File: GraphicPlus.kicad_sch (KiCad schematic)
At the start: 23 parts, among them J1 Apple II Expansion Bus, J2 Printer Connector, Q1 Q_NPN_EBC, SW1 SW_DIP_x04, U1 74LS00, U10 74LS373, U11 74LS373, U2 74LS279, U3 74LS02, U4 74LS00, U5 74LS74, U6 74LS00, U7 74LS08, U8 74LS30, U9 2732

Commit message: native 374 version
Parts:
- removed Q1: Q_NPN_EBC, Package_TO_SOT_THT:TO-92, symbol Device:Q_NPN_EBC
- removed R2: 4.7K, Resistor_THT:R_Axial_DIN0207_L6.3mm_D2.5mm_P10.16mm_Horizontal, symbol Device:R
- removed U4: 74LS00, Package_DIP:DIP-14_W7.62mm, symbol 74xx:74LS00
- added C7, C8: C, Capacitor_THT:C_Rect_L7.0mm_W2.0mm_P5.00mm, symbol Device:C
- C1: value C -> 100p
- C3: value C -> 470p
- D1: footprint Diode_THT:D_A-405_P10.16mm_Horizontal -> Diode_THT:D_A-405_P7.62mm_Horizontal
- U9: value 2732 -> 2764; footprint Package_DIP:DIP-24_W15.24mm -> Package_DIP:DIP-28_W15.24mm; symbol MyEprom:2732 -> Memory_EPROM:2764
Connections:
- net +5V: now also U11.18 (D7), U2.1 (~{R}), U2.2 (~{S1}), U2.3 (~{S2}), U9.1 (VPP), U9.27 (~{PGM}), U9.28 (VCC), C8.1; no longer U9.24 (VCC)
- net A0: now also U9.10 (A0); no longer U9.8 (A0)
- net A1: now also U9.9 (A1); no longer U1.5, U9.7 (A1)
- net A2: now also U9.8 (A2); no longer U1.1, U9.6 (A2)
- net A3: now also U9.7 (A3); no longer U9.5 (A3)
- net A4: now also U9.6 (A4); no longer U9.4 (A4)
- net A5: now also U9.5 (A5); no longer U9.3 (A5)
- net A7: now also U9.3 (A7); no longer U9.1 (A7)
- net ACK: no longer U6.1, U6.2
- net D0: now also U9.11 (D0); no longer U9.9 (D0)
- net D1: now also U9.12 (D1); no longer U9.10 (D1)
- net D2: now also U9.13 (D2); no longer U9.11 (D2)
- net D3: now also U9.15 (D3); no longer U9.13 (D3)
- net D4: now also U9.16 (D4); no longer U9.14 (D4)
- net D5: now also U9.17 (D5); no longer U9.15 (D5)
- net D6: now also U9.18 (D6); no longer U9.16 (D6)
- net D7: now also U9.19 (D7); no longer U9.17 (D7)
- net GND: now also U9.14 (GND), U9.2 (A12), U9.22 (~{OE}), C7.2; no longer U9.12 (GND), U9.18 (~{CE})
- net Q3: now also U3.11
- net ROMA10: now also U9.21 (A10); no longer U9.19 (A10)
- net ROMA11: now also U9.23 (A11); no longer U9.21 (A11)
- net ROMA6: now also U9.4 (A6); no longer U9.2 (A6)
- net ROMA8: now also U9.25 (A8); no longer U9.23 (A8)
- net ROMA9: now also U9.24 (A9); no longer U9.22 (A9)
- net R/~{W}: now also U6.1
- net ~{DEV}: now also U1.4, U1.5
- net ~{ROMEN}: now also C8.2
- net ~{RST}: no longer U2.3 (~{S2})
- net at C1.1, U1.9, U3.1: now also U1.1; no longer U1.2, U1.4
- net ~{BANK2}: now reaches U1.8, U2.15 (~{S1})
- net ~{BANK2}: now also C7.1
- net ~{OUTPUT}: now reaches U2.10 (~{R}), U5.2 (D)
- net ~{OUTPUT}: now also U1.3, U3.12
- net at U3.10: now also U1.2
- net G_OUTPUT: now reaches U10.11 (LE)
- net G_OUTPUT: now also U3.13
- net at U1.6: now also U6.2; no longer U2.2 (~{S1})
- net at U6.3: now also U11.1 (OE); no longer U3.11
- net at U2.4 (Q): no longer U3.12
- removed net IRQ: U11.18 (D7), U3.13
- no-connect marks 18 -> 22
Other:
- note added: "I/O operations Address Read Write C080,y Status Output C081,y Status Select Bank 2 of ROM C082,y Status Reset Interrupt Request and IRQ data bit C084,y Status Output/Interrupt on ACK"
- moved on the sheet: C1, C3, D1, U10, U1A, U1B, U1C, U1D, U2A, U2B, U2C, U2D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

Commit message: consolidate 74ls00 chips, better spacing
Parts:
- J2: footprint Connector_PinHeader_2.54mm:PinHeader_2x13_P2.54mm_Vertical -> Connector_PinHeader_2.54mm:PinHeader_2x13_P2.54mm_Horizontal
- U10: value 74LS373 -> 74LS374; symbol 74xx:74LS373 -> 74xx:74LS374
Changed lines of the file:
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@@
     )
   )
-  (symbol (lib_id "74xx:74LS373") (at 139.7 129.54 0) (unit 1)
+  (symbol (lib_id "74xx:74LS374") (at 139.7 129.54 0) (unit 1)
     (in_bom yes) (on_board yes) (dnp no) (fields_autoplaced)
     (property "Reference" "U10" (at 141.6559 110.49 0)
       (effects (font (size 1.27 1.27)) (justify left))
     )
-    (property "Value" "74LS373" (at 141.6559 113.03 0)
-      (effects (font (size 1.27 1.27)) (justify left))
+    (property "Value" "74LS374" (at 132.08 146.05 0)
+      (effects (font (size 1.27 1.27)))
     )
     (property "Footprint" "Package_DIP:DIP-20_W7.62mm" (at 139.7 129.54 0)
       (effects (font (size 1.27 1.27)) hide)
     )
-    (property "Datasheet" "http://www.ti.com/lit/gpn/sn74LS373" (at 139.7 129.54 0)
+    (property "Datasheet" "http://www.ti.com/lit/gpn/sn74LS374" (at 139.7 129.54 0)
       (effects (font (size 1.27 1.27)) hide)
     )
@@
       (effects (font (size 1.27 1.27)) hide)
     )
-    (property "Footprint" "Connector_PinHeader_2.54mm:PinHeader_2x13_P2.54mm_Vertical" (at 246.38 106.68 0)
-      (effects (font (size 1.27 1.27)) hide)
-    )
+    (property "Footprint" "Connector_PinHeader_2.54mm:PinHeader_2x13_P2.54mm_Horizontal" (at 246.38 106.68 0)
+      (effects (font (size 1.27 1.27)) hide)
+    )

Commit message: finish up rev 1
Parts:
- added U9Alt1: 2732, Package_DIP:DIP-24_W15.24mm, symbol MyEprom:2732
- C2, C4, C5, C6: value C -> 100n
- C7: value C -> 100p
- renumbered SW1 to S1
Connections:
- net +5V: now also U6.10, U6.9, U9Alt1.24 (VCC); no longer U2.2 (~{S1}), U2.3 (~{S2})
- net A0: now also U1.2, U9Alt1.8 (A0); no longer U1.10
- net A1: now also U9Alt1.7 (A1)
- net A2: now also U9Alt1.6 (A2)
- net A3: now also U9Alt1.5 (A3)
- net A4: now also U9Alt1.4 (A4)
- net A5: now also U9Alt1.3 (A5)
- net A7: now also U9Alt1.1 (A7)
- net D0: now also U9Alt1.9 (D0)
- net D1: now also U9Alt1.10 (D1)
- net D2: now also U9Alt1.11 (D2)
- net D3: now also U9Alt1.13 (D3)
- net D4: now also U9Alt1.14 (D4)
- net D5: now also U9Alt1.15 (D5)
- net D6: now also U9Alt1.16 (D6)
- net D7: now also U9Alt1.17 (D7)
- net GND: now also U9.20 (~{CE}), U9Alt1.12 (GND), U9Alt1.18 (~{CE}); no longer U9.22 (~{OE})
- net ROMA10: now also U9Alt1.19 (A10)
- net ROMA11: now also U9Alt1.21 (A11)
- net ROMA6: now also U9Alt1.2 (A6)
- net ROMA8: now also U9Alt1.23 (A8)
- net ROMA9: now also U9Alt1.22 (A9)
- net R/~{W}: now also U6.2; no longer U6.1
- net ~{BANK2}: now also U1.3; no longer U1.8
- net ~{DEV}: now also U6.4, U6.5; no longer U1.4, U1.5
- net ~{IOSEL}: now also U1.4; no longer U6.9
- net ~{IOSTB}: now also U1.5, U2.2 (~{S1}), U2.3 (~{S2}); no longer U6.10, U6.4, U6.5
- net ~{OUTPUT}: now also U6.11; no longer U1.3
- net ~{ROMEN}: now also U1.8, U9.22 (~{OE}), U9Alt1.20 (~{G}VPP); no longer U6.11, U9.20 (~{CE})
- net at C1.1, U1.1, U3.1: now also U6.12; no longer U1.9
- net at U1.6: now also U1.9; no longer U6.2
- net at U8.6: now also U2.4 (Q); no longer U6.6
- net at U6.8: no longer U6.12
- net at U2.7 (Q): now also U1.10; no longer U6.13
- net at U3.10: now also U6.13; no longer U1.2
- new net: U6.1, U6.6
- no-connect marks 22 -> 20
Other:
- moved on the sheet: C1, C7, U1A, U1C, U2A, U2D, U3A, U6B, U6D

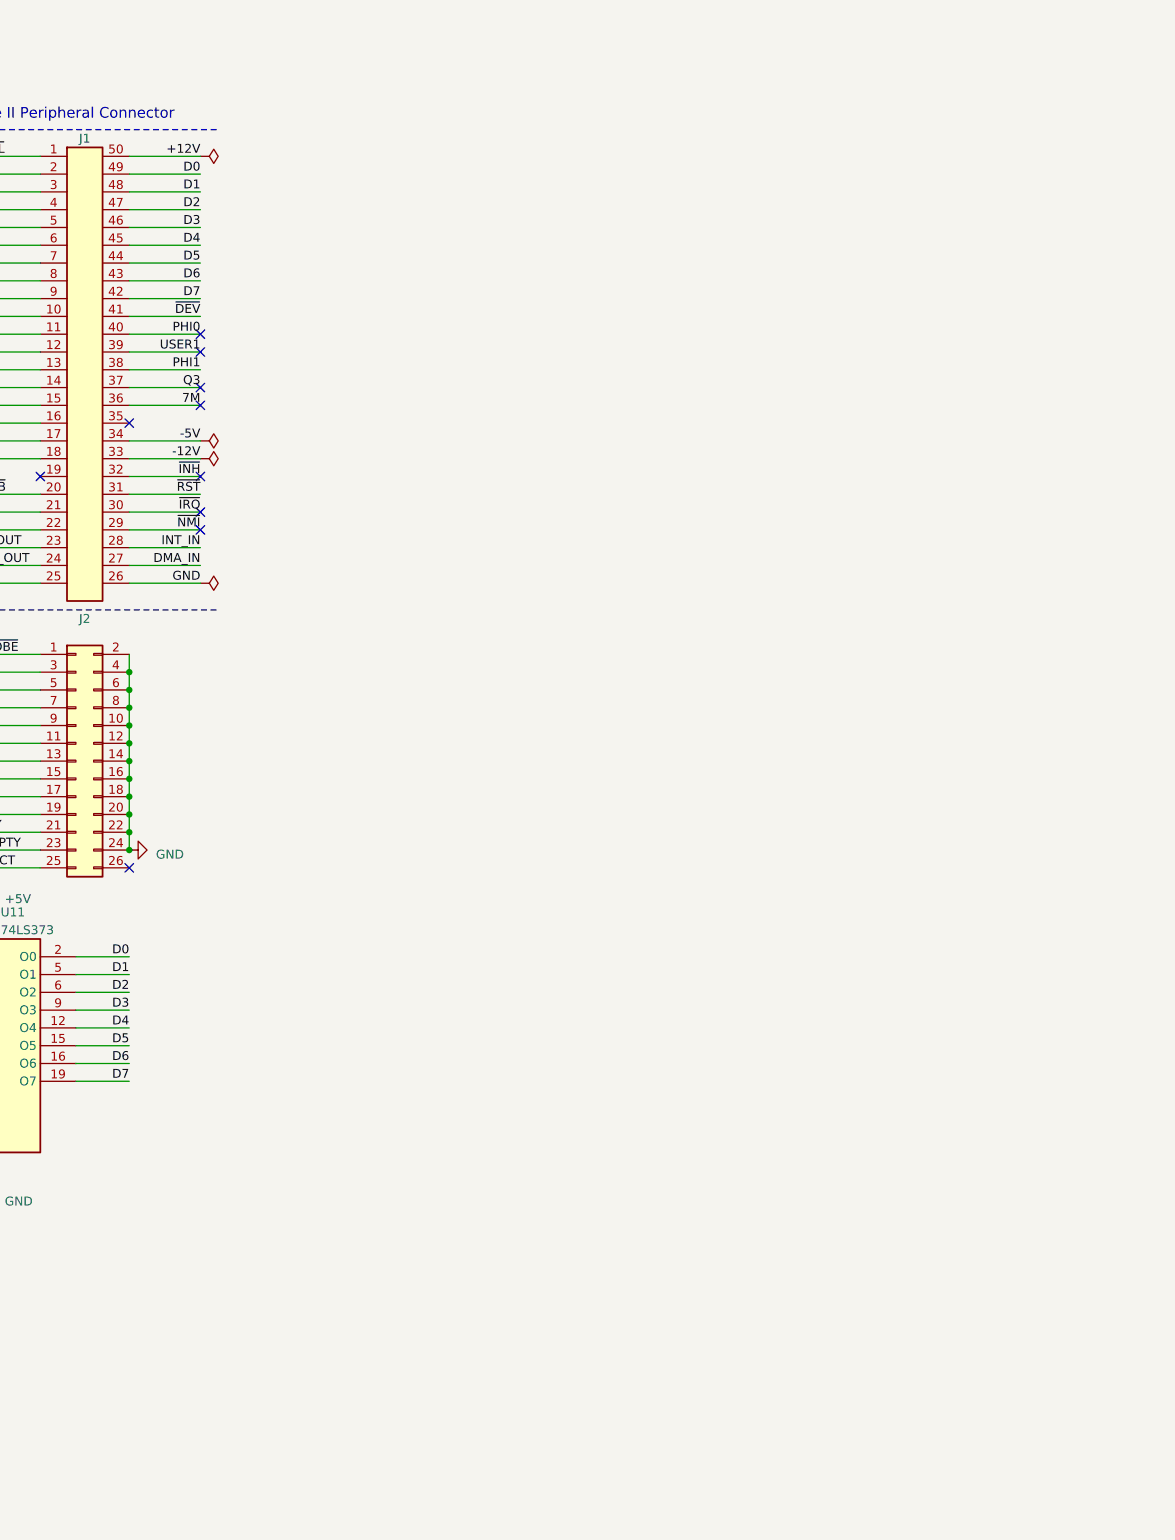
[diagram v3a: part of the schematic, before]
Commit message: rev 2, PC dongle compatibility
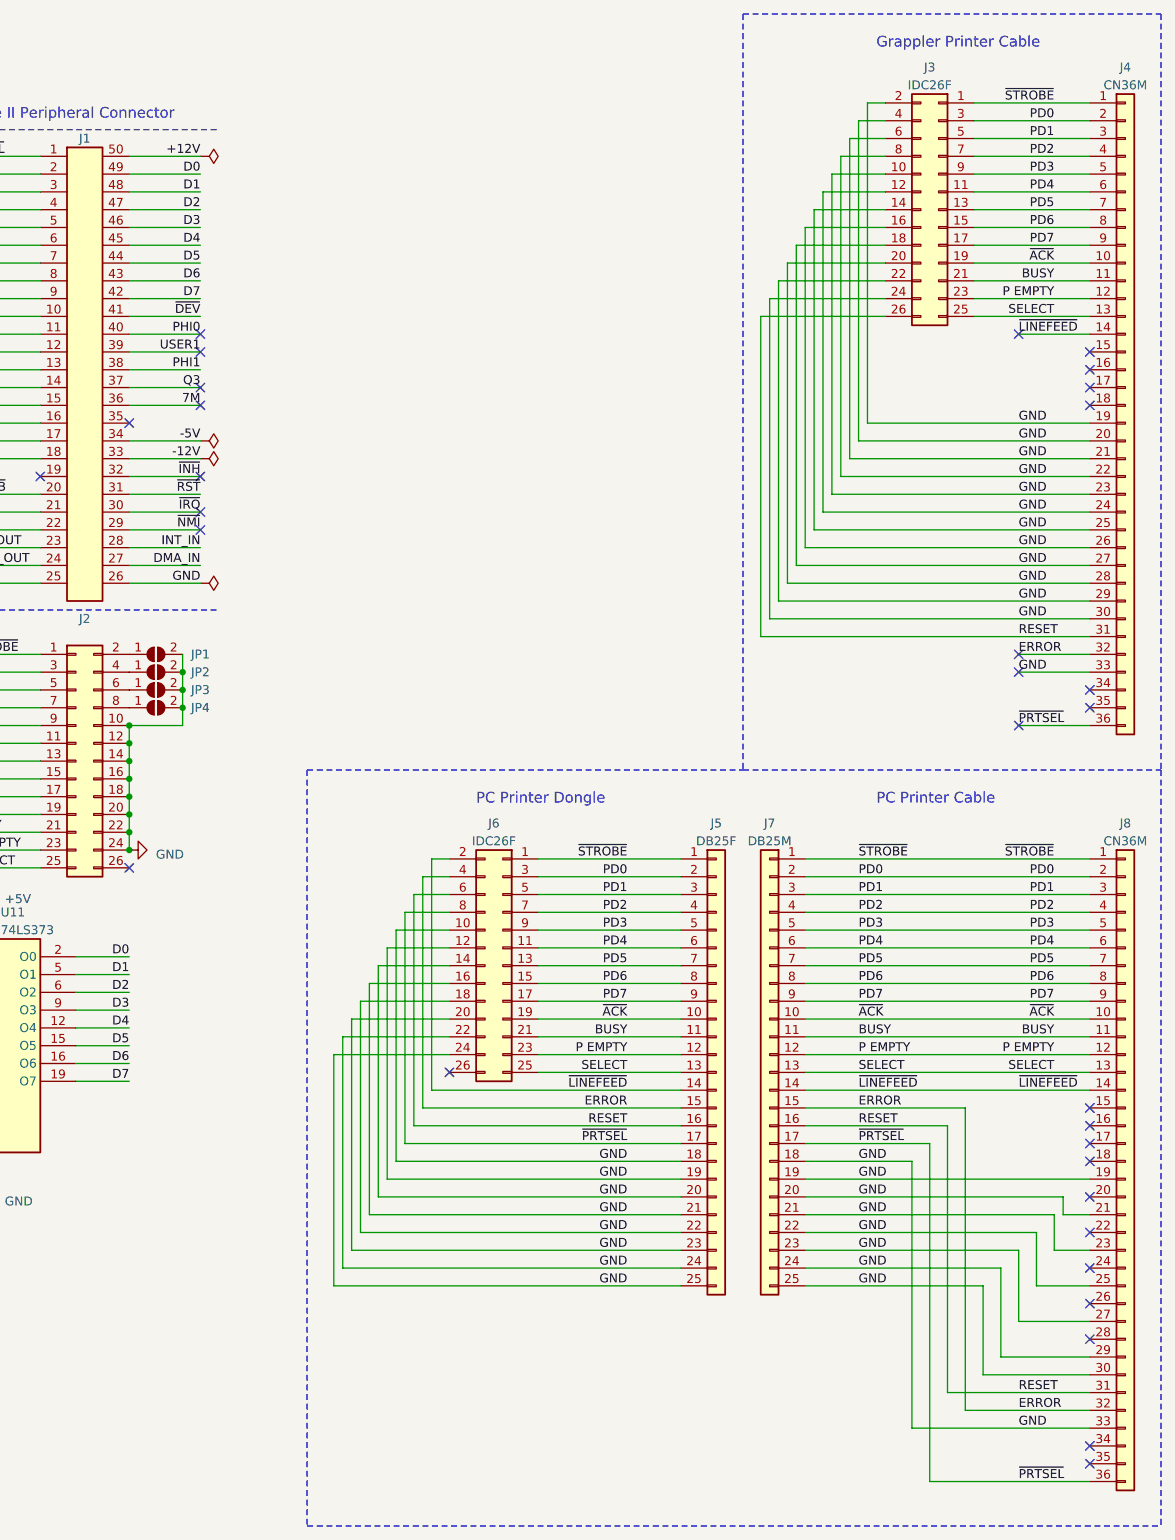
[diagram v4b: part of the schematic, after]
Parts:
- added J3, J6: IDC26F, symbol Connector_Generic:Conn_02x13_Odd_Even
- added J4, J8: CN36M, symbol Connector_Generic:Conn_01x36
- added J5: DB25F, symbol Connector_Generic:Conn_01x25
- added J7: DB25M, symbol Connector_Generic:Conn_01x25
- added JP1, JP2, JP3, JP4: ~, Jumper:SolderJumper-2_P1.3mm_Open_RoundedPad1.0x1.5mm, symbol Jumper:SolderJumper_2_Open
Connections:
- net BUSY: now also J3.21 (Pin_21), J4.11 (Pin_11), J5.11 (Pin_11), J6.21 (Pin_21), J7.11 (Pin_11), J8.11 (Pin_11)
- net GND: now also J3.10 (Pin_10), J3.12 (Pin_12), J3.14 (Pin_14), J3.16 (Pin_16), J3.18 (Pin_18), J3.2 (Pin_2), J3.20 (Pin_20), J3.22 (Pin_22), J3.24 (Pin_24), J3.4 (Pin_4), J3.6 (Pin_6), J3.8 (Pin_8), J4.19 (Pin_19), J4.20 (Pin_20), J4.21 (Pin_21), J4.22 (Pin_22), J4.23 (Pin_23), J4.24 (Pin_24), J4.25 (Pin_25), J4.26 (Pin_26), J4.27 (Pin_27), J4.28 (Pin_28), J4.29 (Pin_29), J4.30 (Pin_30), J4.33 (Pin_33), J5.18 (Pin_18), J5.19 (Pin_19), J5.20 (Pin_20), J5.21 (Pin_21), J5.22 (Pin_22), J5.23 (Pin_23), J5.24 (Pin_24), J5.25 (Pin_25), J6.10 (Pin_10), J6.12 (Pin_12), J6.14 (Pin_14), J6.16 (Pin_16), J6.18 (Pin_18), J6.20 (Pin_20), J6.22 (Pin_22), J6.24 (Pin_24), J7.18 (Pin_18), J7.19 (Pin_19), J7.20 (Pin_20), J7.21 (Pin_21), J7.22 (Pin_22), J7.23 (Pin_23), J7.24 (Pin_24), J7.25 (Pin_25), J8.19 (Pin_19), J8.21 (Pin_21), J8.23 (Pin_23), J8.25 (Pin_25), J8.27 (Pin_27), J8.29 (Pin_29), J8.30 (Pin_30), J8.33 (Pin_33), JP1.2 (B), JP2.2 (B), JP3.2 (B), JP4.2 (B); no longer J2.2 (Pin_2), J2.4 (Pin_4), J2.6 (Pin_6), J2.8 (Pin_8)
- net P EMPTY: now also J3.23 (Pin_23), J4.12 (Pin_12), J5.12 (Pin_12), J6.23 (Pin_23), J7.12 (Pin_12), J8.12 (Pin_12)
- net PD0: now also J3.3 (Pin_3), J4.2 (Pin_2), J5.2 (Pin_2), J6.3 (Pin_3), J7.2 (Pin_2), J8.2 (Pin_2)
- net PD1: now also J3.5 (Pin_5), J4.3 (Pin_3), J5.3 (Pin_3), J6.5 (Pin_5), J7.3 (Pin_3), J8.3 (Pin_3)
- net PD2: now also J3.7 (Pin_7), J4.4 (Pin_4), J5.4 (Pin_4), J6.7 (Pin_7), J7.4 (Pin_4), J8.4 (Pin_4)
- net PD3: now also J3.9 (Pin_9), J4.5 (Pin_5), J5.5 (Pin_5), J6.9 (Pin_9), J7.5 (Pin_5), J8.5 (Pin_5)
- net PD4: now also J3.11 (Pin_11), J4.6 (Pin_6), J5.6 (Pin_6), J6.11 (Pin_11), J7.6 (Pin_6), J8.6 (Pin_6)
- net PD5: now also J3.13 (Pin_13), J4.7 (Pin_7), J5.7 (Pin_7), J6.13 (Pin_13), J7.7 (Pin_7), J8.7 (Pin_7)
- net PD6: now also J3.15 (Pin_15), J4.8 (Pin_8), J5.8 (Pin_8), J6.15 (Pin_15), J7.8 (Pin_8), J8.8 (Pin_8)
- net PD7: now also J3.17 (Pin_17), J4.9 (Pin_9), J5.9 (Pin_9), J6.17 (Pin_17), J7.9 (Pin_9), J8.9 (Pin_9)
- net SELECT: now also J3.25 (Pin_25), J4.13 (Pin_13), J5.13 (Pin_13), J6.25 (Pin_25), J7.13 (Pin_13), J8.13 (Pin_13)
- net ~{ACK}: now also J3.19 (Pin_19), J4.10 (Pin_10), J5.10 (Pin_10), J6.19 (Pin_19), J7.10 (Pin_10), J8.10 (Pin_10)
- net ~{STROBE}: now also J3.1 (Pin_1), J4.1 (Pin_1), J5.1 (Pin_1), J6.1 (Pin_1), J7.1 (Pin_1), J8.1 (Pin_1)
- new net: J2.8 (Pin_8), JP4.1 (A)
- new net: J2.4 (Pin_4), JP2.1 (A)
- new net: J2.6 (Pin_6), JP3.1 (A)
- new net: J2.2 (Pin_2), JP1.1 (A)
- new net ERROR: J4.32 (Pin_32), J5.15 (Pin_15), J6.4 (Pin_4), J7.15 (Pin_15), J8.32 (Pin_32)
- new net RESET: J3.26 (Pin_26), J4.31 (Pin_31), J5.16 (Pin_16), J6.6 (Pin_6), J7.16 (Pin_16), J8.31 (Pin_31)
- new net ~{LINEFEED}: J4.14 (Pin_14), J5.14 (Pin_14), J6.2 (Pin_2), J7.14 (Pin_14), J8.14 (Pin_14)
- new net ~{PRTSEL}: J4.36 (Pin_36), J5.17 (Pin_17), J6.8 (Pin_8), J7.17 (Pin_17), J8.36 (Pin_36)
- no-connect marks 20 -> 42
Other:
- note added: "Grappler Printer Cable"
- note added: "PC Printer Cable"
- note added: "PC Printer Dongle"

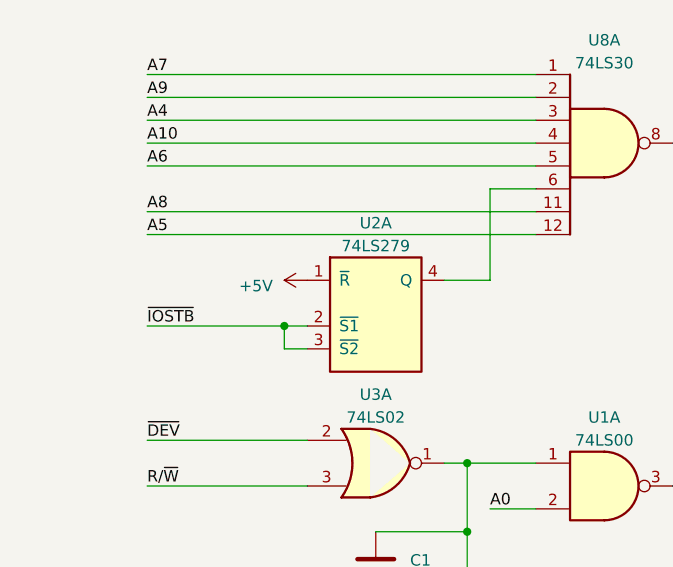
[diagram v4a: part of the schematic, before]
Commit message: U2 pin 1 supposed to be GND, not +5
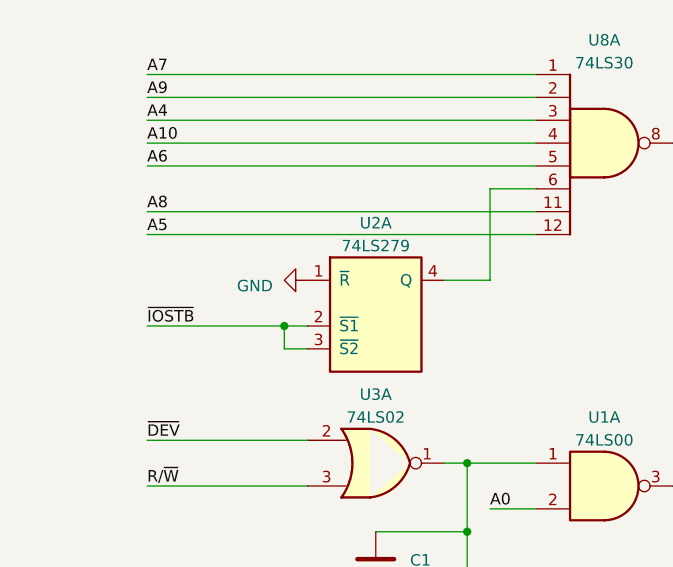
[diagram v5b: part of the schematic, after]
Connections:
- net +5V: no longer U2.1 (~{R})
- net GND: now also U2.1 (~{R})
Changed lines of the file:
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@@
   (title_block
     (date "2023-09-21")
-    (rev "2")
+    (rev "3")
   )
   (junction (at 175.26 144.78) (diameter 0) (color 0 0 0 0)
@@
     )
   )
+  (symbol (lib_id "power:GND") (at 43.18 48.26 270) (unit 1)
+    (in_bom yes) (on_board yes) (dnp no) (fields_autoplaced)
+    (property "Reference" "#PWR042" (at 36.83 48.26 0)
+      (effects (font (size 1.27 1.27)) hide)
+    )
+    (property "Value" "GND" (at 39.37 48.895 90)
+      (effects (font (size 1.27 1.27)) (justify right))
+    )
+    (property "Footprint" "" (at 43.18 48.26 0)
+      (effects (font (size 1.27 1.27)) hide)
+    )
+    (property "Datasheet" "" (at 43.18 48.26 0)
+      (effects (font (size 1.27 1.27)) hide)
+    )
+    (pin "1")
+    (instances
+      (project "GraphicPlus"
+        (path "/e35c56f9-4713-4571-acdb-6ae2f2073fad"
+          (reference "#PWR042") (unit 1)
+        )
+      )
+    )
+  )
   (symbol (lib_id "power:GND") (at 88.9 198.12 0) (unit 1)
     (in_bom yes) (on_board yes) (dnp no) (fields_autoplaced)
@@
         )
       )
-    )
-  )
-  (symbol (lib_id "power:+5V") (at 43.18 48.26 90) (mirror x) (unit 1)
-    (in_bom yes) (on_board yes) (dnp no) (fields_autoplaced)
-    (property "Reference" "#PWR042" (at 46.99 48.26 0)
-      (effects (font (size 1.27 1.27)) hide)
-    )
-    (property "Value" "+5V" (at 39.37 48.895 90)
-      (effects (font (size 1.27 1.27)) (justify left))
-    )
-    (property "Footprint" "" (at 43.18 48.26 0)
-      (effects (font (size 1.27 1.27)) hide)
-    )
-    (property "Datasheet" "" (at 43.18 48.26 0)
-      (effects (font (size 1.27 1.27)) hide)
-    )
-    (pin "1")
-    (instances
-      (project "GraphicPlus"
-        (path "/e35c56f9-4713-4571-acdb-6ae2f2073fad"
-          (reference "#PWR042") (unit 1)
-        )
-      )

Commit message: rev3 fixes
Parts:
- removed J3, J6: IDC26F, symbol Connector_Generic:Conn_02x13_Odd_Even
- removed J4, J8: CN36M, symbol Connector_Generic:Conn_01x36
- removed J5: DB25F, symbol Connector_Generic:Conn_01x25
- removed J7: DB25M, symbol Connector_Generic:Conn_01x25
- C8: value C -> 100p
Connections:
- net +5V: now also U9.26 (NC)
- no-connect marks 42 -> 20
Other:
- added sheet Cables (cables.kicad_sch)
- note removed: "Grappler Printer Cable"
- note removed: "PC Printer Cable"
- note removed: "PC Printer Dongle"
